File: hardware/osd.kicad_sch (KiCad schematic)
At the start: 12 parts, among them U14 SN74LVC1G3157, U15 TLV7031

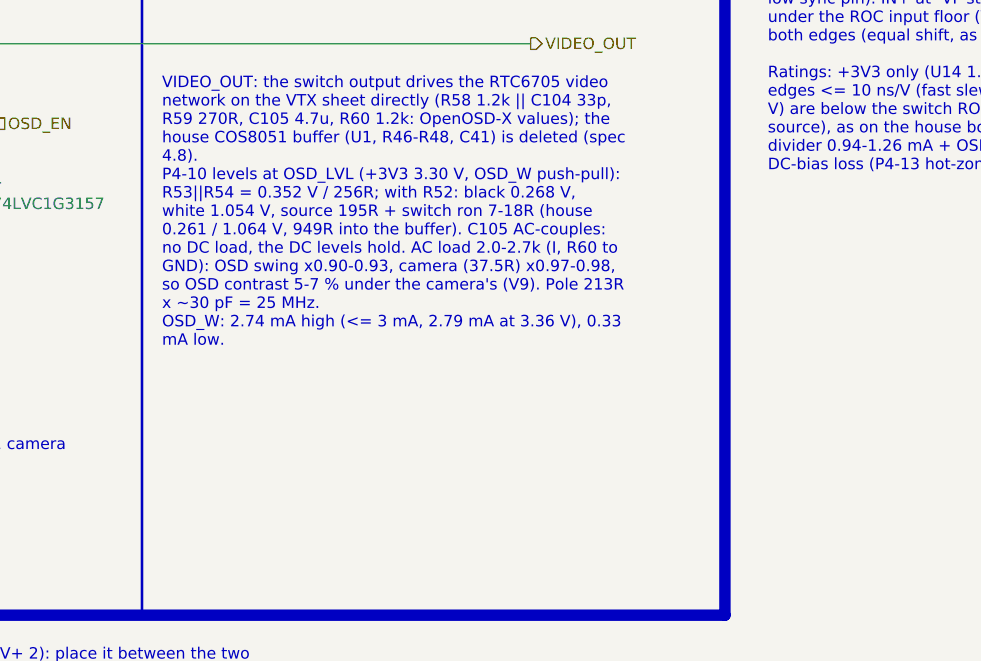
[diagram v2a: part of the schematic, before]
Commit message: schematic: integrated (ERC 0 errors / 2 justified warnings; check_netlist 7/7; conventions 0 FAIL; visual 0 hits; 268/268 refs match bom_plan; FC+RX pin maps match PINMAP)
Co-Authored-By: Claude Opus 5.5 <noreply@anthropic.com>
Claude-Session: https://claude.ai/code/session_01RFaS5jnC9tnPam9GBgmGnG
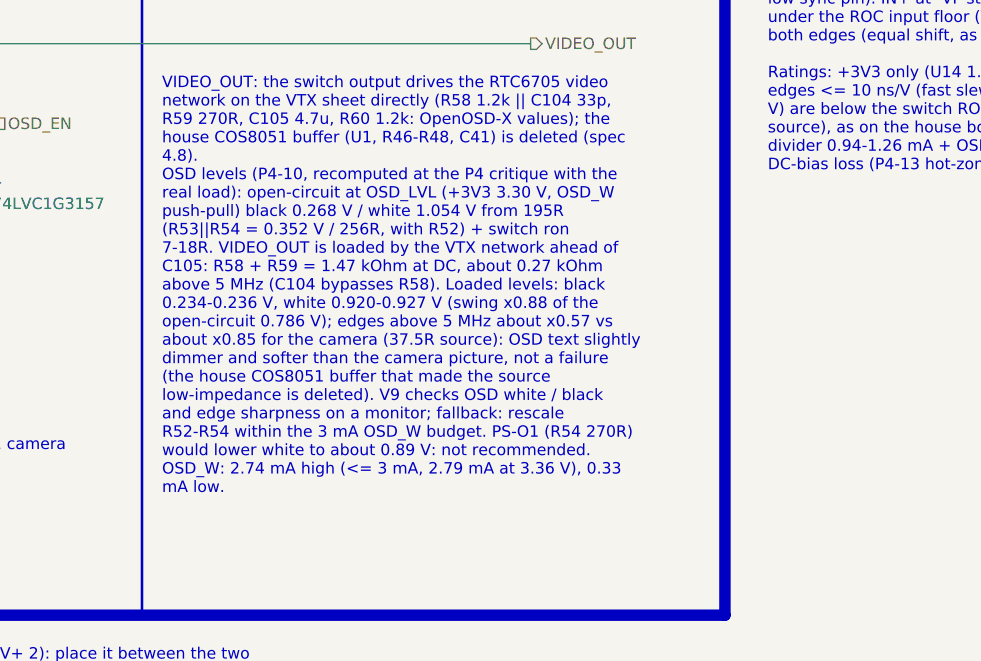
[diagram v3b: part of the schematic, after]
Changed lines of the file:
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@@
 		)
 	)
-	(text_box "VIDEO_OUT: the switch output drives the RTC6705 video network on the VTX sheet directly (R58 1.2k || C104 33p, R59 270R, C105 4.7u, R60 1.2k: OpenOSD-X values); the house COS8051 buffer (U1, R46-R48, C41) is deleted (spec 4.8).\nP4-10 levels at OSD_LVL (+3V3 3.30 V, OSD_W push-pull): R53||R54 = 0.352 V / 256R; with R52: black 0.268 V, white 1.054 V, source 195R + switch ron 7-18R (house 0.261 / 1.064 V, 949R into the buffer). C105 AC-couples: no DC load, the DC levels hold. AC load 2.0-2.7k (I, R60 to GND): OSD swing x0.90-0.93, camera (37.5R) x0.97-0.98, so OSD contrast 5-7 % under the camera's (V9). Pole 213R x ~30 pF = 25 MHz.\nOSD_W: 2.74 mA high (<= 3 mA, 2.79 mA at 3.36 V), 0.33 mA low."
+	(text_box "VIDEO_OUT: the switch output drives the RTC6705 video network on the VTX sheet directly (R58 1.2k || C104 33p, R59 270R, C105 4.7u, R60 1.2k: OpenOSD-X values); the house COS8051 buffer (U1, R46-R48, C41) is deleted (spec 4.8).\nOSD levels (P4-10, recomputed at the P4 critique with the real load): open-circuit at OSD_LVL (+3V3 3.30 V, OSD_W push-pull) black 0.268 V / white 1.054 V from 195R (R53||R54 = 0.352 V / 256R, with R52) + switch ron 7-18R. VIDEO_OUT is loaded by the VTX network ahead of C105: R58 + R59 = 1.47 kOhm at DC, about 0.27 kOhm above 5 MHz (C104 bypasses R58). Loaded levels: black 0.234-0.236 V, white 0.920-0.927 V (swing x0.88 of the open-circuit 0.786 V); edges above 5 MHz about x0.57 vs about x0.85 for the camera (37.5R source): OSD text slightly dimmer and softer than the camera picture, not a failure (the house COS8051 buffer that made the source low-impedance is deleted). V9 checks OSD white / black and edge sharpness on a monitor; fallback: rescale R52-R54 within the 3 mA OSD_W budget. PS-O1 (R54 270R) would lower white to about 0.89 V: not recommended.\nOSD_W: 2.74 mA high (<= 3 mA, 2.79 mA at 3.36 V), 0.33 mA low."
 		(exclude_from_sim no)
 		(at 133.35 86.36 0)
@@
 		(in_pos_files no)
 		(dnp no)
-		(property "Reference" "#PWR142"
+		(property "Reference" "#PWR147"
 			(at 158.75 69.85 0)
 			(hide yes)
@@
 			(project "OpenAIO-Whoop"
 				(path "/2c3a7206-1e66-4d43-a02f-491225e20dd6/d622c956-8c4e-5ac1-b8c4-8a8024f124d6"
-					(reference "#PWR142")
+					(reference "#PWR147")
 					(unit 1)
 				)
@@
 			)
 		)
-		(property "Description" ""
+		(property "Description" "[project copy of OpenDrone:SDM02U30LP3-7B with datasheet pin types, P4 integration 2026-10-09]"
 			(at 125.73 60.96 0)
 			(hide yes)
@@
 		(in_pos_files no)
 		(dnp no)
-		(property "Reference" "#PWR143"
+		(property "Reference" "#PWR148"
 			(at 54.61 72.39 0)
 			(hide yes)
@@
 			(project "OpenAIO-Whoop"
 				(path "/2c3a7206-1e66-4d43-a02f-491225e20dd6/d622c956-8c4e-5ac1-b8c4-8a8024f124d6"
-					(reference "#PWR143")
+					(reference "#PWR148")
 					(unit 1)
 				)
@@
 		(in_pos_files no)
 		(dnp no)
-		(property "Reference" "#PWR152"
+		(property "Reference" "#PWR157"
 			(at 106.68 119.38 0)
 			(hide yes)
@@
 			(project "OpenAIO-Whoop"
 				(path "/2c3a7206-1e66-4d43-a02f-491225e20dd6/d622c956-8c4e-5ac1-b8c4-8a8024f124d6"
-					(reference "#PWR152")
+					(reference "#PWR157")
 					(unit 1)
 				)
@@
 		(in_pos_files no)
 		(dnp no)
-		(property "Reference" "#PWR144"
+		(property "Reference" "#PWR149"
 			(at 63.5 72.39 0)
 			(hide yes)
@@
 			(project "OpenAIO-Whoop"
 				(path "/2c3a7206-1e66-4d43-a02f-491225e20dd6/d622c956-8c4e-5ac1-b8c4-8a8024f124d6"
-					(reference "#PWR144")
+					(reference "#PWR149")
 					(unit 1)
 				)
@@
 		(in_pos_files no)
 		(dnp no)
-		(property "Reference" "#PWR153"
+		(property "Reference" "#PWR158"
 			(at 66.04 135.89 0)
 			(hide yes)
@@
 			(project "OpenAIO-Whoop"
 				(path "/2c3a7206-1e66-4d43-a02f-491225e20dd6/d622c956-8c4e-5ac1-b8c4-8a8024f124d6"
-					(reference "#PWR153")
+					(reference "#PWR158")
 					(unit 1)
 				)
@@
 		(in_pos_files no)
 		(dnp no)
-		(property "Reference" "#PWR141"
+		(property "Reference" "#PWR146"
 			(at 184.15 59.69 0)
 			(hide yes)
@@
 			(project "OpenAIO-Whoop"
 				(path "/2c3a7206-1e66-4d43-a02f-491225e20dd6/d622c956-8c4e-5ac1-b8c4-8a8024f124d6"
-					(reference "#PWR141")
+					(reference "#PWR146")
 					(unit 1)
 				)
@@
 			)
 		)
-		(property "Description" "Nanopower push-pull comparator in X2SON package."
+		(property "Description" "Nanopower push-pull comparator in X2SON package. [project copy of OpenDrone:TLV7031DPWR with datasheet pin types, P4 integration 2026-10-09]"
 			(at 167.64 58.42 0)
 			(hide yes)
@@
 		(in_pos_files no)
 		(dnp no)
-		(property "Reference" "#PWR149"
+		(property "Reference" "#PWR154"
 			(at 106.68 93.98 0)
 			(hide yes)
@@
 			(project "OpenAIO-Whoop"
 				(path "/2c3a7206-1e66-4d43-a02f-491225e20dd6/d622c956-8c4e-5ac1-b8c4-8a8024f124d6"
-					(reference "#PWR149")
+					(reference "#PWR154")
 					(unit 1)
 				)
@@
 		(in_pos_files no)
 		(dnp no)
-		(property "Reference" "#PWR151"
+		(property "Reference" "#PWR156"
 			(at 66.04 113.03 0)
 			(hide yes)
@@
 			(project "OpenAIO-Whoop"
 				(path "/2c3a7206-1e66-4d43-a02f-491225e20dd6/d622c956-8c4e-5ac1-b8c4-8a8024f124d6"
-					(reference "#PWR151")
+					(reference "#PWR156")
 					(unit 1)
 				)
@@
 			)
 		)
-		(property "Description" ""
+		(property "Description" "[project copy of OpenDrone:SN74LVC1G3157DTBR with datasheet pin types, P4 integration 2026-10-09]"
 			(at 106.68 101.6 0)
 			(hide yes)
@@
 		(in_pos_files no)
 		(dnp no)
-		(property "Reference" "#PWR146"
+		(property "Reference" "#PWR151"
 			(at 125.73 72.39 0)
 			(hide yes)
@@
 			(project "OpenAIO-Whoop"
 				(path "/2c3a7206-1e66-4d43-a02f-491225e20dd6/d622c956-8c4e-5ac1-b8c4-8a8024f124d6"
-					(reference "#PWR146")
+					(reference "#PWR151")
 					(unit 1)
 				)
@@
 		(in_pos_files no)
 		(dnp no)
-		(property "Reference" "#PWR150"
+		(property "Reference" "#PWR155"
 			(at 91.44 100.33 0)
 			(hide yes)
@@
 			(project "OpenAIO-Whoop"
 				(path "/2c3a7206-1e66-4d43-a02f-491225e20dd6/d622c956-8c4e-5ac1-b8c4-8a8024f124d6"
-					(reference "#PWR150")
+					(reference "#PWR155")
 					(unit 1)
 				)
@@
 		(in_pos_files no)
 		(dnp no)
-		(property "Reference" "#PWR148"
+		(property "Reference" "#PWR153"
 			(at 91.44 90.17 0)
 			(hide yes)
@@
 			(project "OpenAIO-Whoop"
 				(path "/2c3a7206-1e66-4d43-a02f-491225e20dd6/d622c956-8c4e-5ac1-b8c4-8a8024f124d6"
-					(reference "#PWR148")
+					(reference "#PWR153")
 					(unit 1)
 				)
@@
 		(in_pos_files no)
 		(dnp no)
-		(property "Reference" "#PWR145"
+		(property "Reference" "#PWR150"
 			(at 93.98 72.39 0)
 			(hide yes)
@@
 			(project "OpenAIO-Whoop"
 				(path "/2c3a7206-1e66-4d43-a02f-491225e20dd6/d622c956-8c4e-5ac1-b8c4-8a8024f124d6"
-					(reference "#PWR145")
+					(reference "#PWR150")
 					(unit 1)
 				)
@@
 		(in_pos_files no)
 		(dnp no)
-		(property "Reference" "#PWR147"
+		(property "Reference" "#PWR152"
 			(at 176.53 72.39 0)
 			(hide yes)
@@
 			(project "OpenAIO-Whoop"
 				(path "/2c3a7206-1e66-4d43-a02f-491225e20dd6/d622c956-8c4e-5ac1-b8c4-8a8024f124d6"
-					(reference "#PWR147")
+					(reference "#PWR152")
 					(unit 1)
 				)

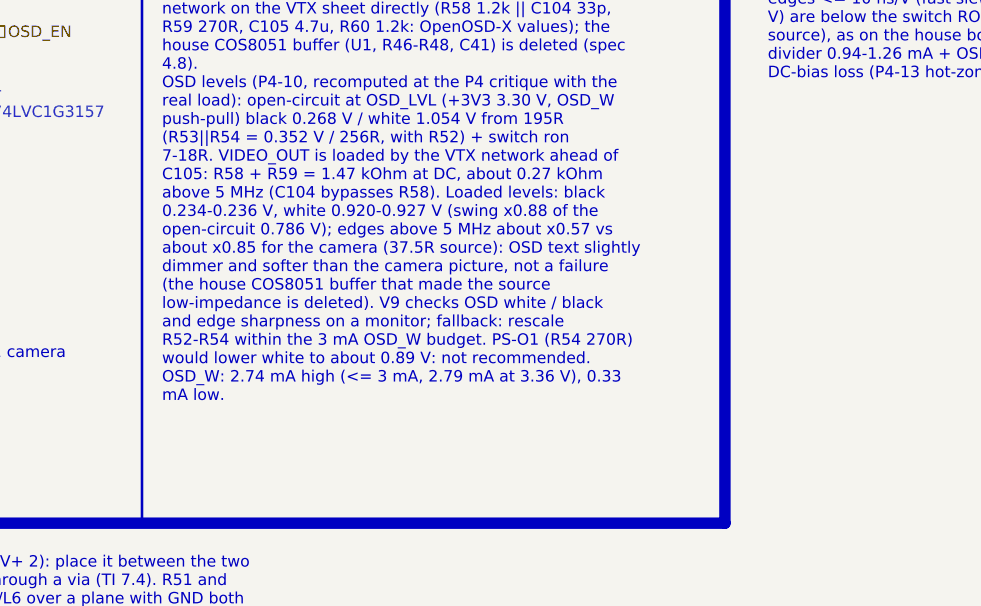
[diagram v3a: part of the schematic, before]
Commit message: hardware: floorplan v3 review pass (RX RF corner blocker fixed; majors listed in FLOORPLAN.md Open)
Co-Authored-By: Claude Opus 5.5 <noreply@anthropic.com>
Claude-Session: https://claude.ai/code/session_01RFaS5jnC9tnPam9GBgmGnG
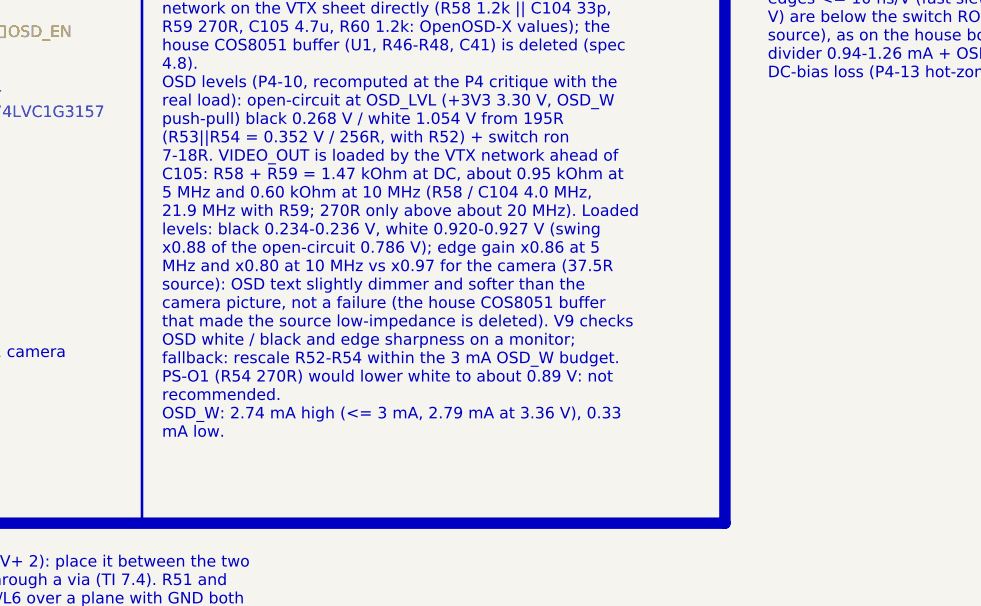
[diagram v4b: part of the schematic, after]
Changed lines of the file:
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@@
 		)
 	)
-	(text_box "VIDEO_OUT: the switch output drives the RTC6705 video network on the VTX sheet directly (R58 1.2k || C104 33p, R59 270R, C105 4.7u, R60 1.2k: OpenOSD-X values); the house COS8051 buffer (U1, R46-R48, C41) is deleted (spec 4.8).\nOSD levels (P4-10, recomputed at the P4 critique with the real load): open-circuit at OSD_LVL (+3V3 3.30 V, OSD_W push-pull) black 0.268 V / white 1.054 V from 195R (R53||R54 = 0.352 V / 256R, with R52) + switch ron 7-18R. VIDEO_OUT is loaded by the VTX network ahead of C105: R58 + R59 = 1.47 kOhm at DC, about 0.27 kOhm above 5 MHz (C104 bypasses R58). Loaded levels: black 0.234-0.236 V, white 0.920-0.927 V (swing x0.88 of the open-circuit 0.786 V); edges above 5 MHz about x0.57 vs about x0.85 for the camera (37.5R source): OSD text slightly dimmer and softer than the camera picture, not a failure (the house COS8051 buffer that made the source low-impedance is deleted). V9 checks OSD white / black and edge sharpness on a monitor; fallback: rescale R52-R54 within the 3 mA OSD_W budget. PS-O1 (R54 270R) would lower white to about 0.89 V: not recommended.\nOSD_W: 2.74 mA high (<= 3 mA, 2.79 mA at 3.36 V), 0.33 mA low."
+	(text_box "VIDEO_OUT: the switch output drives the RTC6705 video network on the VTX sheet directly (R58 1.2k || C104 33p, R59 270R, C105 4.7u, R60 1.2k: OpenOSD-X values); the house COS8051 buffer (U1, R46-R48, C41) is deleted (spec 4.8).\nOSD levels (P4-10, recomputed at the P4 critique with the real load): open-circuit at OSD_LVL (+3V3 3.30 V, OSD_W push-pull) black 0.268 V / white 1.054 V from 195R (R53||R54 = 0.352 V / 256R, with R52) + switch ron 7-18R. VIDEO_OUT is loaded by the VTX network ahead of C105: R58 + R59 = 1.47 kOhm at DC, about 0.95 kOhm at 5 MHz and 0.60 kOhm at 10 MHz (R58 / C104 4.0 MHz, 21.9 MHz with R59; 270R only above about 20 MHz). Loaded levels: black 0.234-0.236 V, white 0.920-0.927 V (swing x0.88 of the open-circuit 0.786 V); edge gain x0.86 at 5 MHz and x0.80 at 10 MHz vs x0.97 for the camera (37.5R source): OSD text slightly dimmer and softer than the camera picture, not a failure (the house COS8051 buffer that made the source low-impedance is deleted). V9 checks OSD white / black and edge sharpness on a monitor; fallback: rescale R52-R54 within the 3 mA OSD_W budget. PS-O1 (R54 270R) would lower white to about 0.89 V: not recommended.\nOSD_W: 2.74 mA high (<= 3 mA, 2.79 mA at 3.36 V), 0.33 mA low."
 		(exclude_from_sim no)
 		(at 133.35 86.36 0)

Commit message: schematic: review complete (4 rounds; U20 pin 1 to GND, footprint filters fixed, TPS22810DRVR, R54 270R); ERC 0 errors, check_netlist 7/7; D85-D87
Co-Authored-By: Claude Opus 5.5 <noreply@anthropic.com>
Claude-Session: https://claude.ai/code/session_01RFaS5jnC9tnPam9GBgmGnG
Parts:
- R54: value 287R -> 270R; MPN RC0201FR-07287RL -> RC0201FR-07270RL
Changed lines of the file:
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@@
 			)
 		)
-		(property "Value" "287R"
+		(property "Value" "270R"
 			(at 62.23 124.46 0)
 			(show_name no)
@@
 			)
 		)
-		(property "MPN" "RC0201FR-07287RL"
+		(property "MPN" "RC0201FR-07270RL"
 			(at 66.04 125.73 0)
 			(hide yes)

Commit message: WIP final schematic (D111/D113): GPIO map, D100 oscillator, final footprints, lineup power-net names; mid-run snapshot, not yet verified (ERC/netlist/DRU regen pending)
Co-Authored-By: Claude Opus 5.5 <noreply@anthropic.com>
Claude-Session: https://claude.ai/code/session_01RFaS5jnC9tnPam9GBgmGnG
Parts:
- C66, C67, C68, C70: footprint lib:C_0201_0603Metric_W -> lib:C_0201_0603Metric_L
- R51, R52, R53, R54, R55: footprint lib:R_0201_0603Metric_W -> lib:R_0201_0603Metric_L
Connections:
- net +3V3 renamed +3.3V

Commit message: WIP final schematic (D111/D113): further sheet and doc updates, PDF re-export; mid-run snapshot, not yet verified
Co-Authored-By: Claude Opus 5.5 <noreply@anthropic.com>
Claude-Session: https://claude.ai/code/session_01RFaS5jnC9tnPam9GBgmGnG
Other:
- note added: "Comparator: OSD_SYNC low during sync, read by RP2354A PIO2 (GPIO23)"
- note removed: "Comparator: OSD_SYNC low during sync, read by RP2354A PIO2 (GPIO16)"
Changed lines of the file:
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@@
 		)
 	)
-	(text "Comparator: OSD_SYNC low during sync,\nread by RP2354A PIO2 (GPIO16)"
+	(text "Comparator: OSD_SYNC low during sync,\nread by RP2354A PIO2 (GPIO23)"
 		(exclude_from_sim no)
 		(at 164.338 74.676 0)
